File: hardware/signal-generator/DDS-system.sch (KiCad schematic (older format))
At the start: 18 parts, among them U1 74HC04, U10 MCP23017-E/SO, U11 AD9764AR, U12 TS4061AICT-1.25, U8 DS1085Z-10+, U9 CY7C1021D-10ZSXI

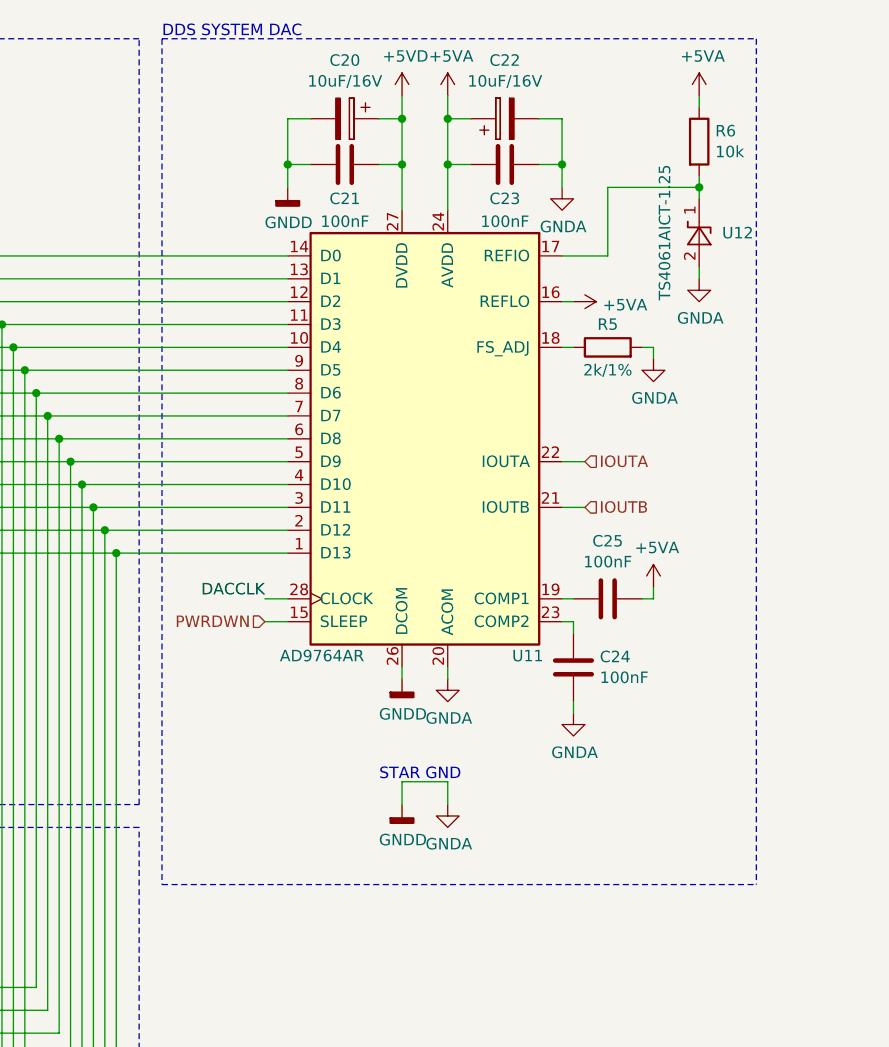
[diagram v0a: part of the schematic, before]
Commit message: [Signal Generator] Decouple voltage references with capacitors
Both the AZ431-A (+2.5V) and the TS4061 (+1.25V) voltage references have
been decoupled to GND with 100nF capacitors.
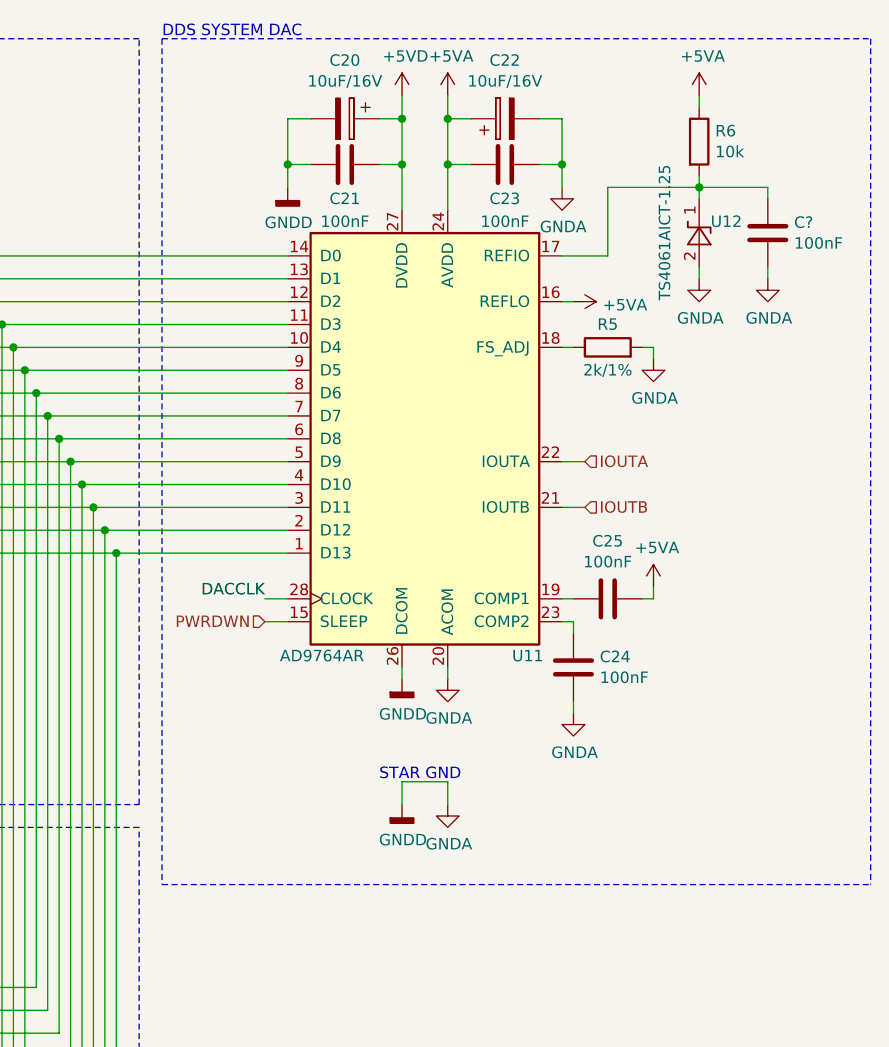
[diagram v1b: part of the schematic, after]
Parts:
- added C?: 100nF, symbol Device:C
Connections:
- net GNDA: now also C?.2
- net at R6.2, U11.17 (REFIO), U12.1 (K): now also C?.1
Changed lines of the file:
@@
 Sheet 2 6
 Title "Digital Function Generator v2 - DDS System"
-Date "2019-12-15"
+Date "2019-12-20"
 Rev "1"
 Comp "Petar Nikolov"
@@
 U 1 1 5DFE0B4C
 P 9300 1600
-F 0 "U12" V 9300 1500 50  0000 R CNN
+F 0 "U12" V 9350 1550 50  0000 R CNN
 F 1 "TS4061AICT-1.25" H 9600 1750 50  0000 R CNN
 F 2 "TO_SOT_Packages_SMD:SOT-323_SC-70_Handsoldering" H 9300 1400 50  0001 C CIN
@@
 Wire Wire Line
 	8700 1700 8900 1700
-Wire Notes Line
-	9550 750  9550 4450
-Wire Notes Line
-	6950 4450 9550 4450
-Wire Notes Line
-	6950 750  9550 750
 Wire Wire Line
 	9300 1400 9300 1350
@@
 	0    1    1    0
 $EndComp
+$Comp
+L Device:C C?
+U 1 1 5DFEC1DC
+P 9600 1600
+F 0 "C?" H 9715 1646 50  0000 L CNN
+F 1 "100nF" H 9715 1555 50  0000 L CNN
+F 2 "" H 9638 1450 50  0001 C CNN
+F 3 "~" H 9600 1600 50  0001 C CNN
+	1    9600 1600
+	1    0    0    -1
+$EndComp
+Wire Wire Line
+	9600 1450 9600 1400
+Wire Wire Line
+	9600 1400 9300 1400
+Wire Wire Line
+	9600 1750 9600 1800
+$Comp
+L power:GNDA #PWR?
+U 1 1 5DFFFA9B
+P 9600 1800
+F 0 "#PWR?" H 9600 1550 50  0001 C CNN
+F 1 "GNDA" H 9605 1627 50  0000 C CNN
+F 2 "" H 9600 1800 50  0001 C CNN
+F 3 "" H 9600 1800 50  0001 C CNN
+	1    9600 1800
+	1    0    0    -1
+$EndComp
+Wire Notes Line
+	10050 750  10050 4450
+Wire Notes Line
+	6950 4450 10050 4450
+Wire Notes Line
+	6950 750  10050 750
 $EndSCHEMATC

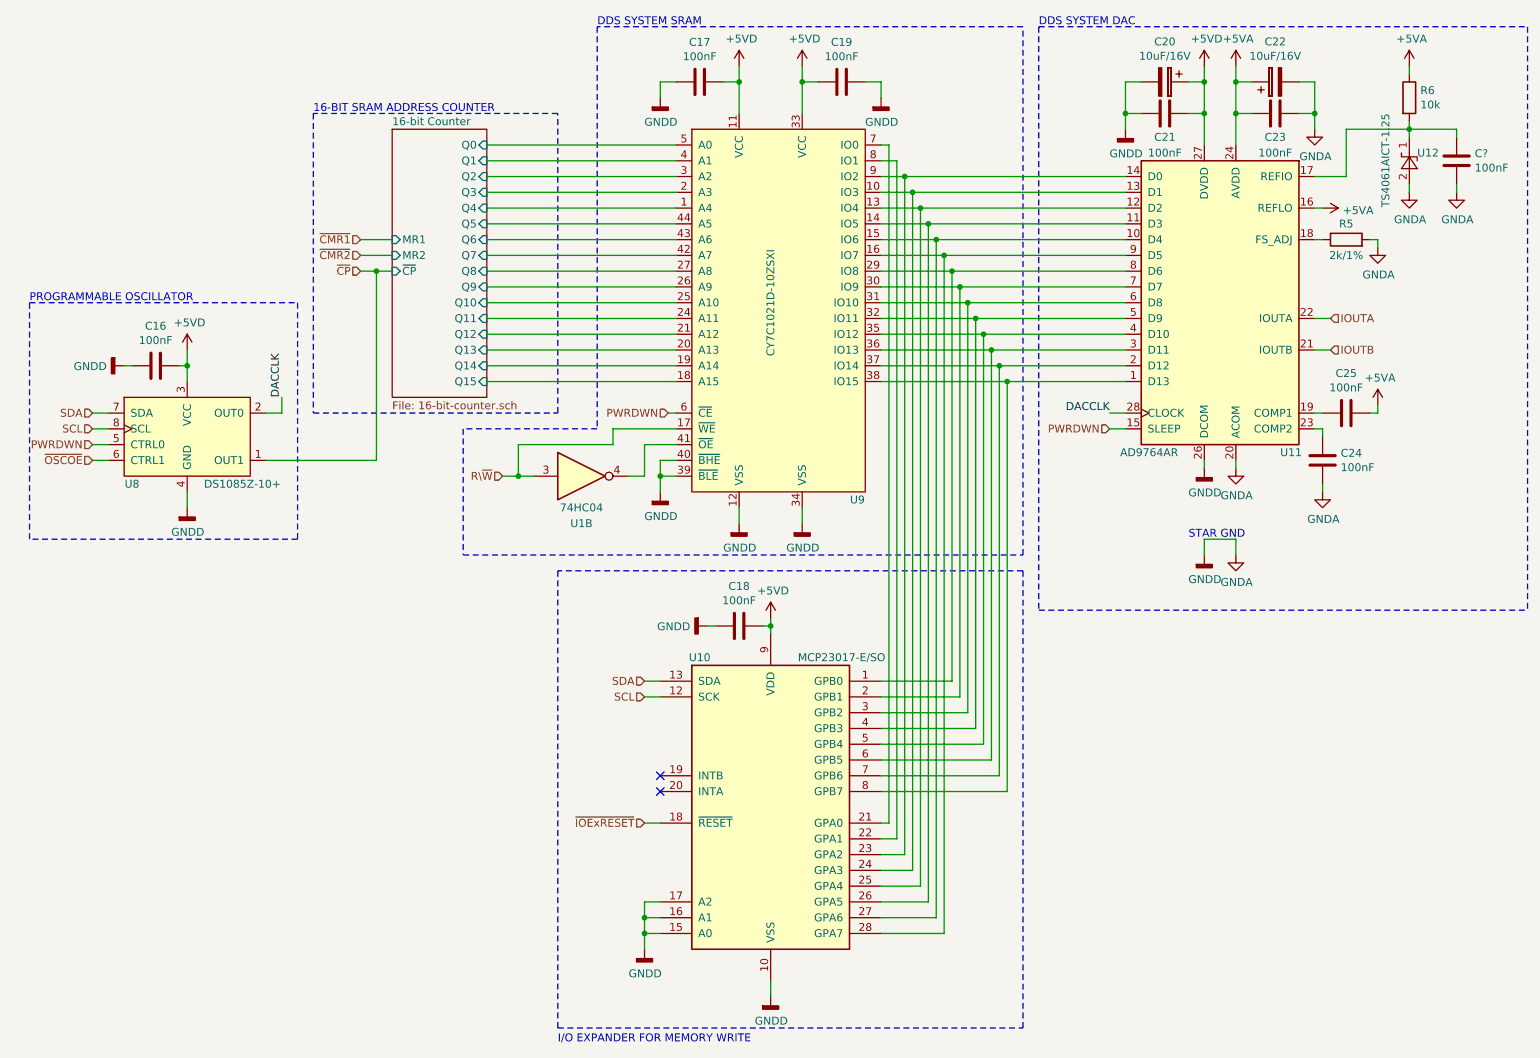
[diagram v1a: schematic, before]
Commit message: [Signal Generator] Change LCD backlight control method
The LCD's backlight was previously intended to be controlled via a
digital potentiometer. However, a much more elegant solution is to
control said backlight via PWM.

Also, removed the level shifter schematic sheet. The level shifters have been
moved to the TFT module's schematic sheet.
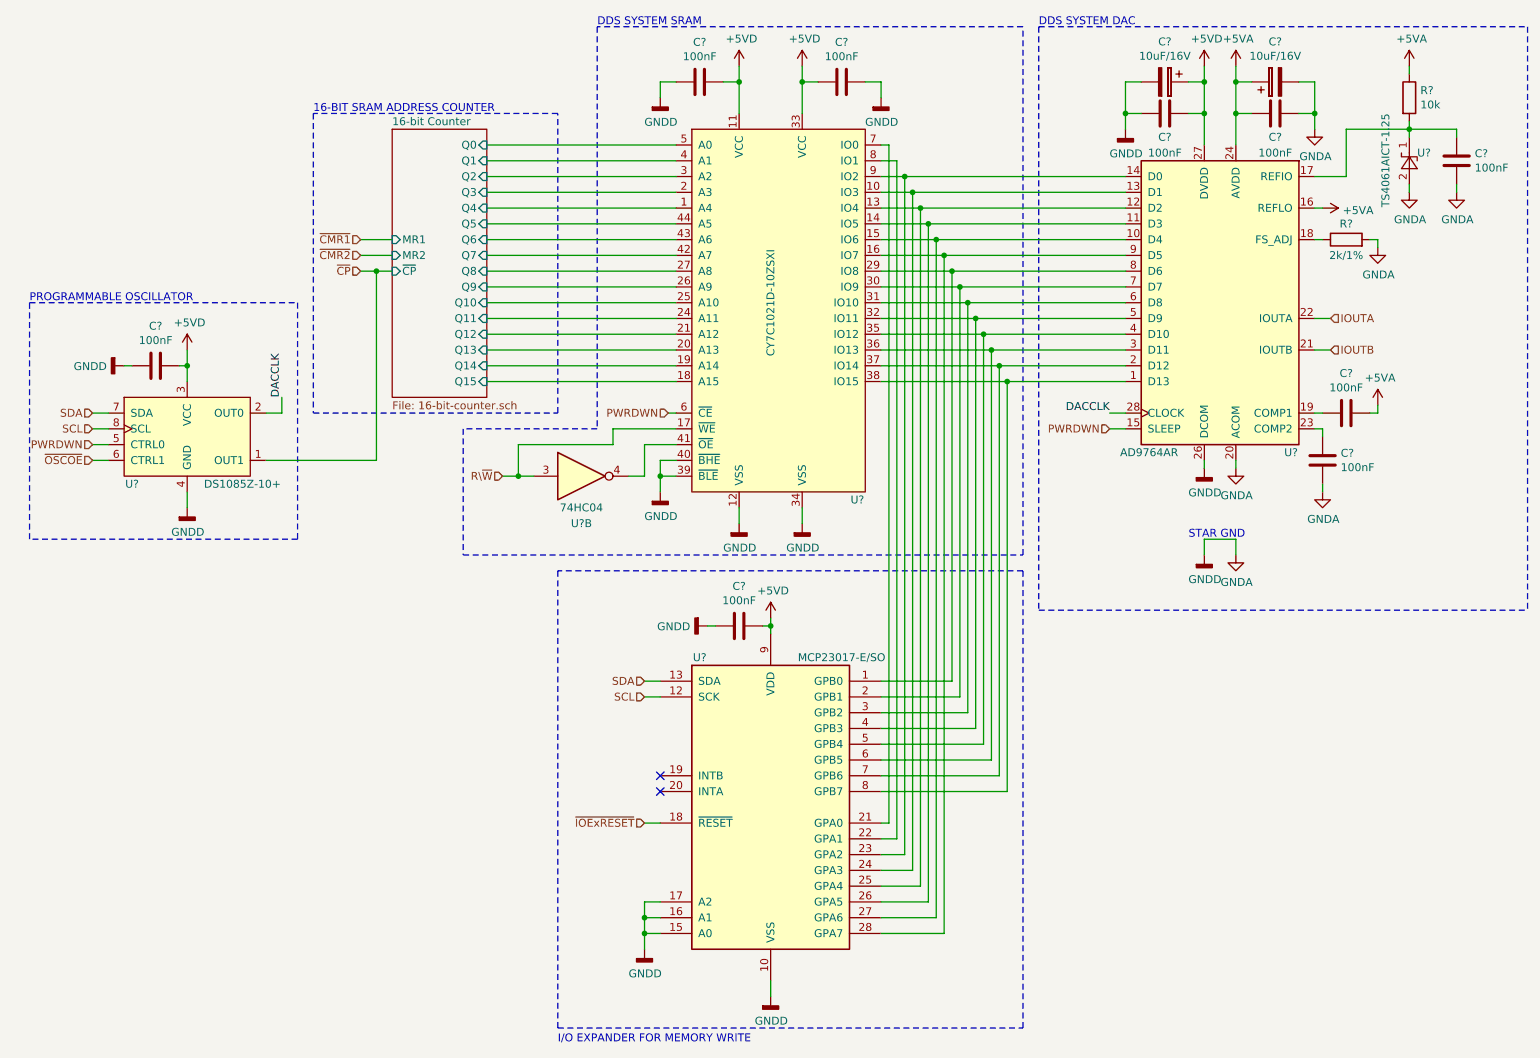
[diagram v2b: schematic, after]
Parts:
- renumbered C16 to C?, C17 to C?, C19 to C?, C25 to C?, C24 to C?, C23 to C?, C22 to C?, C21 to C?, C20 to C?, C18 to C?, R5 to R?, R6 to R?, U10 to U?, U1 to U?, U11 to U?, U9 to U?, U8 to U?, U12 to U?

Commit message: [Signal Generator] Finalize schematic
The electronic schematic is now finalized. All components have been
annotated. Furthermore, all components have an appropriate footprint
associated to them.
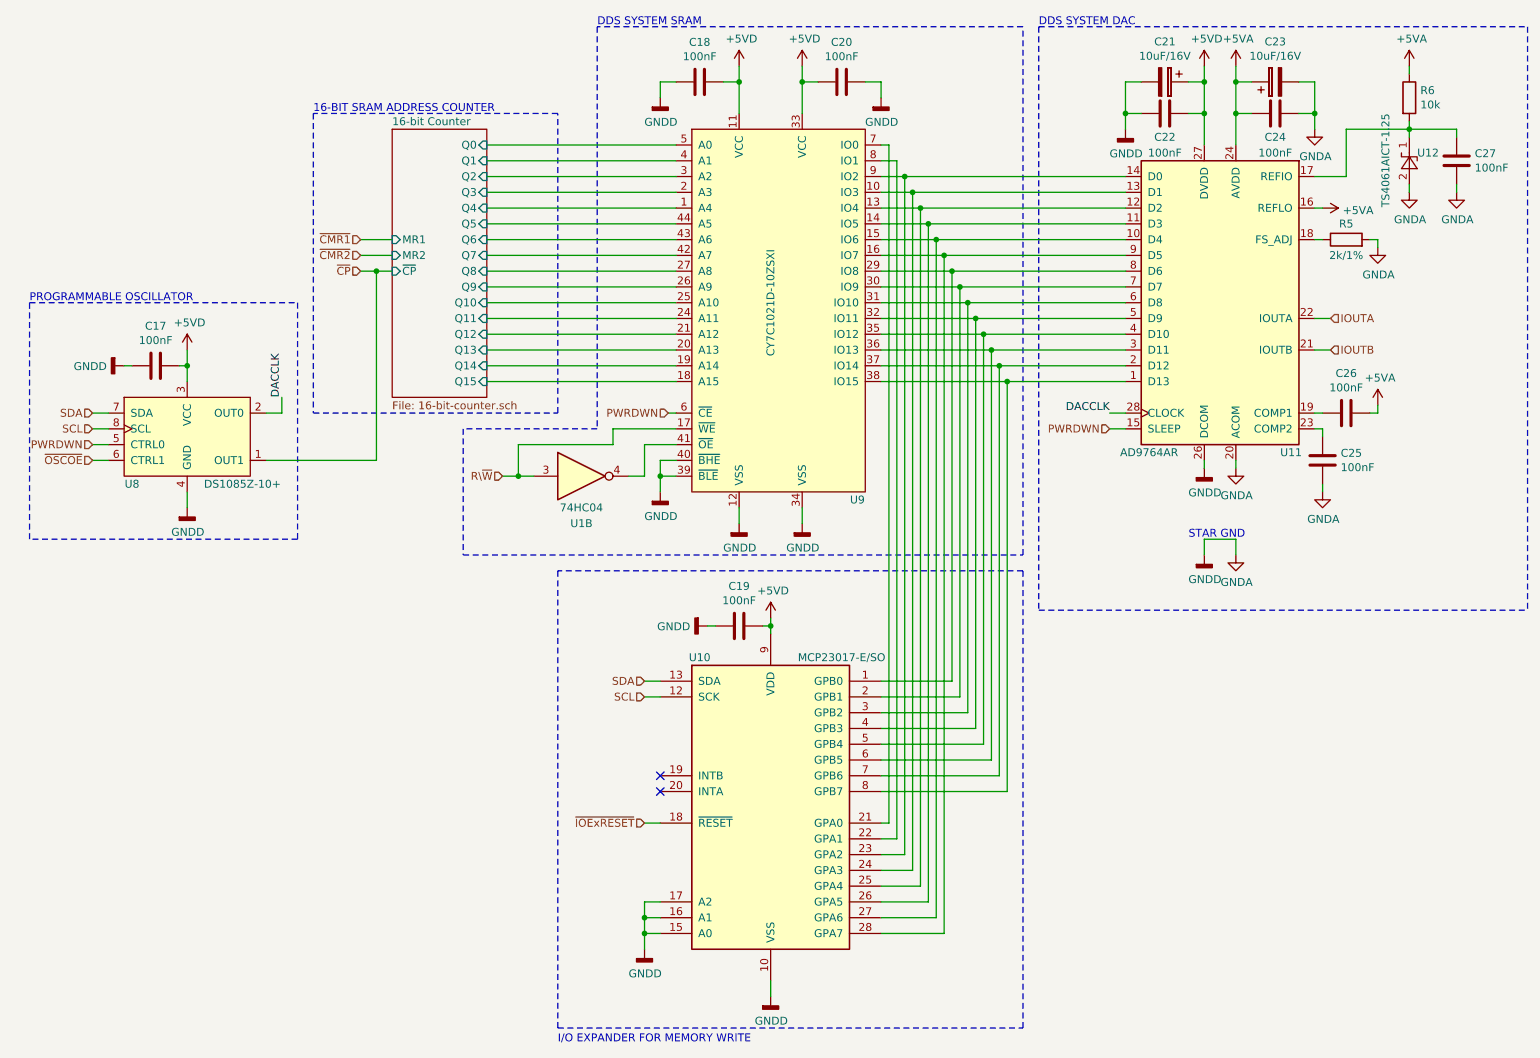
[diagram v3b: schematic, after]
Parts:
- C27: renamed from C?; footprint (none) -> Capacitors_SMD:C_0805_HandSoldering
- gave numbers to parts that had none: 18
